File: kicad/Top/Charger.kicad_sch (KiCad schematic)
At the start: 37 parts

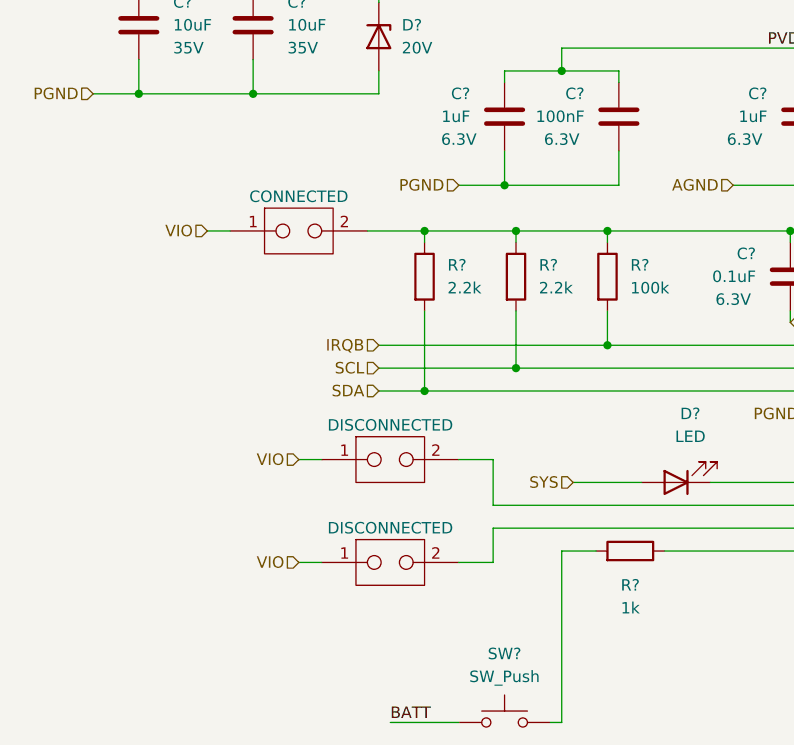
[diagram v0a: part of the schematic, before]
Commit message: replaced all shunt jumpers with better symbols
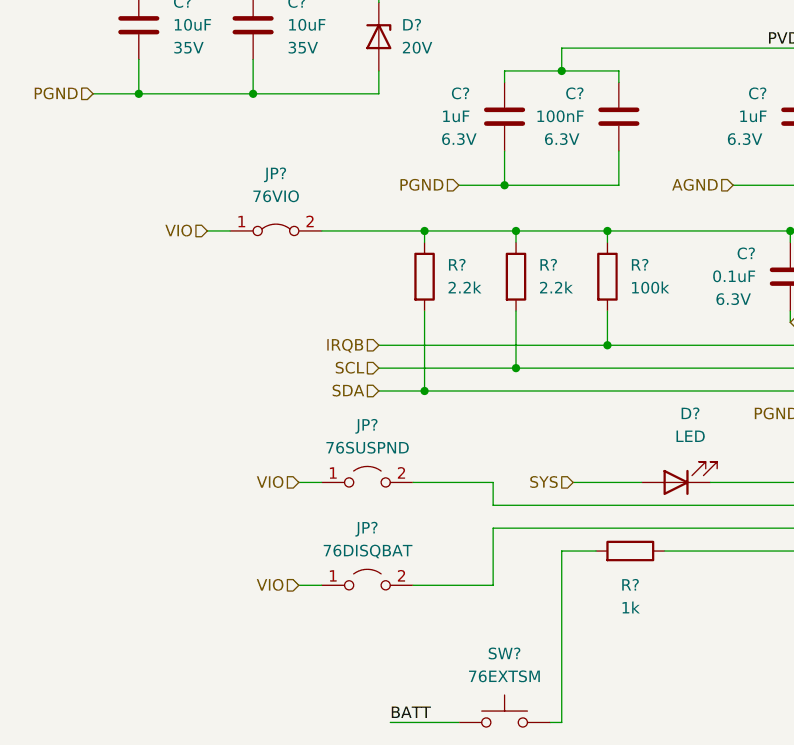
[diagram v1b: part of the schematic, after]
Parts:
- removed CHG_DISQBAT, CHG_SUSPND: DISCONNECTED, custom_connectors:2.54mm_2pointCurrentTestPoint, symbol custom_connectors:TestPoint_CurrentShunt
- removed CHG_VIO: CONNECTED, custom_connectors:2.54mm_2pointCurrentTestPoint, symbol custom_connectors:TestPoint_CurrentShunt
- added JP?: 76SUSPND, custom_connectors:2.54mm_2pointCurrentTestPoint, symbol Jumper:Jumper_2_Open
- added JP?: 76DISQBAT, custom_connectors:2.54mm_2pointCurrentTestPoint, symbol Jumper:Jumper_2_Open
- added JP?: 76VIO, custom_connectors:2.54mm_2pointCurrentTestPoint, symbol Jumper:Jumper_2_Bridged
- SW?: value SW_Push -> 76EXTSM
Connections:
- net VIO: now also JP?.1 (A), JP?.1 (A), JP?.1 (A)
- net at U?.1 (DISQBAT): now also JP?.2 (B)
- net at C?.1, R?.1, R?.1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: now also JP?.2 (B)
- net at U?.31 (SUSPND): now also JP?.2 (B)
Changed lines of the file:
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@@
+    (stroke (width 0) (type default) (color 0 0 0 0))
+  )
+  (wire (pts (xy 57.15 139.7) (xy 57.15 137.16))
     (stroke (width 0) (type default) (color 0 0 0 0))
   )
@@
     (stroke (width 0) (type default) (color 0 0 0 0))
   )
-  (wire (pts (xy 43.18 109.22) (xy 49.53 109.22))
+  (wire (pts (xy 38.1 109.22) (xy 49.53 109.22))
     (stroke (width 0) (type default) (color 0 0 0 0))
   )
@@
     (stroke (width 0) (type default) (color 0 0 0 0))
   )
-  (wire (pts (xy 57.15 134.62) (xy 57.15 139.7))
-    (stroke (width 0) (type default) (color 0 0 0 0))
-  )
   (wire (pts (xy 147.32 109.22) (xy 147.32 111.76))
     (stroke (width 0) (type default) (color 0 0 0 0))
@@
     (stroke (width 0) (type default) (color 0 0 0 0))
   )
-  (wire (pts (xy 53.34 134.62) (xy 57.15 134.62))
-    (stroke (width 0) (type default) (color 0 0 0 0))
-  )
   (wire (pts (xy 170.18 142.24) (xy 170.18 139.7))
     (stroke (width 0) (type default) (color 0 0 0 0))
@@
     (stroke (width 0) (type default) (color 0 0 0 0))
   )
-  (wire (pts (xy 57.15 142.24) (xy 57.15 146.05))
+  (wire (pts (xy 57.15 142.24) (xy 57.15 148.59))
     (stroke (width 0) (type default) (color 0 0 0 0))
   )
@@
     (stroke (width 0) (type default) (color 0 0 0 0))
   )
+  (wire (pts (xy 57.15 148.59) (xy 48.26 148.59))
+    (stroke (width 0) (type default) (color 0 0 0 0))
+  )
   (wire (pts (xy 147.32 124.46) (xy 147.32 127))
     (stroke (width 0) (type default) (color 0 0 0 0))
@@
     (stroke (width 0) (type default) (color 0 0 0 0))
   )
+  (wire (pts (xy 57.15 137.16) (xy 48.26 137.16))
+    (stroke (width 0) (type default) (color 0 0 0 0))
+  )
   (wire (pts (xy 168.91 152.4) (xy 170.18 152.4))
     (stroke (width 0) (type default) (color 0 0 0 0))
@@
     (stroke (width 0) (type default) (color 0 0 0 0))
   )
-  (wire (pts (xy 35.56 134.62) (xy 38.1 134.62))
+  (wire (pts (xy 35.56 137.16) (xy 38.1 137.16))
     (stroke (width 0) (type default) (color 0 0 0 0))
   )
@@
     (stroke (width 0) (type default) (color 0 0 0 0))
   )
-  (wire (pts (xy 57.15 146.05) (xy 53.34 146.05))
-    (stroke (width 0) (type default) (color 0 0 0 0))
-  )
   (wire (pts (xy 264.16 106.68) (xy 264.16 109.22))
     (stroke (width 0) (type default) (color 0 0 0 0))
@@
     (stroke (width 0) (type default) (color 0 0 0 0))
   )
-  (wire (pts (xy 35.56 146.05) (xy 38.1 146.05))
+  (wire (pts (xy 35.56 148.59) (xy 38.1 148.59))
     (stroke (width 0) (type default) (color 0 0 0 0))
   )
@@
     (effects (font (size 1.27 1.27)) (justify right))
   )
-  (hierarchical_label "VIO" (shape input) (at 35.56 134.62 180)
+  (hierarchical_label "VIO" (shape input) (at 35.56 137.16 180)
     (effects (font (size 1.27 1.27)) (justify right))
   )
@@
     (effects (font (size 1.27 1.27)) (justify left))
   )
-  (hierarchical_label "VIO" (shape input) (at 35.56 146.05 180)
+  (hierarchical_label "VIO" (shape input) (at 35.56 148.59 180)
     (effects (font (size 1.27 1.27)) (justify right))
   )
@@
   (hierarchical_label "IRQB" (shape input) (at 44.45 121.92 180)
     (effects (font (size 1.27 1.27)) (justify right))
-  )
-  (symbol (lib_id "custom_connectors:TestPoint_CurrentShunt") (at 45.72 146.05 0) (unit 1)
-    (in_bom yes) (on_board yes) (fields_autoplaced)
-    (property "Reference" "CHG_DISQBAT" (id 0) (at 45.72 140.97 0)
-      (effects (font (size 1.27 1.27)) hide)
-    )
-    (property "Value" "DISCONNECTED" (id 1) (at 45.72 142.24 0))
-    (property "Footprint" "custom_connectors:2.54mm_2pointCurrentTestPoint" (id 2) (at 45.72 146.05 0)
-      (effects (font (size 1.27 1.27)) hide)
-    )
-    (property "Datasheet" "https://www.digikey.jp/product-detail/en/kycon-inc/SX1100-B/2092-SX1100-B-ND/9990206" (id 3) (at 45.72 146.05 0)
-      (effects (font (size 1.27 1.27)) hide)
-    )
-    (pin "1")
-    (pin "2")
   )
   (symbol (lib_id "Device:C") (at 191.77 128.27 0) (mirror y) (unit 1)
@@
     (pin "2")
   )
+  (symbol (lib_id "Jumper:Jumper_2_Open") (at 43.18 137.16 0) (unit 1)
+    (in_bom yes) (on_board yes) (fields_autoplaced)
+    (property "Reference" "JP?" (id 0) (at 43.18 130.81 0))
+    (property "Value" "76SUSPND" (id 1) (at 43.18 133.35 0))
+    (property "Footprint" "custom_connectors:2.54mm_2pointCurrentTestPoint" (id 2) (at 43.18 137.16 0)
+      (effects (font (size 1.27 1.27)) hide)
+    )
+    (property "Datasheet" "~" (id 3) (at 43.18 137.16 0)
+      (effects (font (size 1.27 1.27)) hide)
+    )
+    (property "Description" "2.54mm male header with jumper absent" (id 4) (at 43.18 137.16 0)
+      (effects (font (size 1.27 1.27)) hide)
+    )
+    (pin "1")
+    (pin "2")
+  )
+  (symbol (lib_id "Jumper:Jumper_2_Open") (at 43.18 148.59 0) (unit 1)
+    (in_bom yes) (on_board yes) (fields_autoplaced)
+    (property "Reference" "JP?" (id 0) (at 43.18 142.24 0))
+    (property "Value" "76DISQBAT" (id 1) (at 43.18 144.78 0))
+    (property "Footprint" "custom_connectors:2.54mm_2pointCurrentTestPoint" (id 2) (at 43.18 148.59 0)
+      (effects (font (size 1.27 1.27)) hide)
+    )
+    (property "Datasheet" "~" (id 3) (at 43.18 148.59 0)
+      (effects (font (size 1.27 1.27)) hide)
+    )
+    (property "Description" "2.54mm male header with jumper absent" (id 4) (at 43.18 148.59 0)
+      (effects (font (size 1.27 1.27)) hide)
+    )
+    (pin "1")
+    (pin "2")
+  )
   (symbol (lib_id "pspice:INDUCTOR") (at 171.45 99.06 0) (unit 1)
     (in_bom yes) (on_board yes)
@@
     (pin "2")
   )
+  (symbol (lib_id "Jumper:Jumper_2_Bridged") (at 33.02 109.22 0) (unit 1)
+    (in_bom yes) (on_board yes) (fields_autoplaced)
+    (property "Reference" "JP?" (id 0) (at 33.02 102.87 0))
+    (property "Value" "76VIO" (id 1) (at 33.02 105.41 0))
+    (property "Footprint" "custom_connectors:2.54mm_2pointCurrentTestPoint" (id 2) (at 33.02 109.22 0)
+      (effects (font (size 1.27 1.27)) hide)
+    )
+    (property "Datasheet" "~" (id 3) (at 33.02 109.22 0)
+      (effects (font (size 1.27 1.27)) hide)
+    )
+    (property "Description" "2.54mm male header with jumper attached" (id 4) (at 33.02 109.22 0)
+      (effects (font (size 1.27 1.27)) hide)
+    )
+    (pin "1")
+    (pin "2")
+  )
   (symbol (lib_id "Connector:TestPoint") (at 91.44 81.28 0) (unit 1)
     (in_bom yes) (on_board yes) (fields_autoplaced)
@@
     )
     (property "Description" "6.3V" (id 4) (at 53.34 99.06 0))
-    (pin "1")
-    (pin "2")
-  )
-  (symbol (lib_id "custom_connectors:TestPoint_CurrentShunt") (at 35.56 109.22 0) (unit 1)
-    (in_bom yes) (on_board yes) (fields_autoplaced)
-    (property "Reference" "CHG_VIO" (id 0) (at 35.56 104.14 0)
-      (effects (font (size 1.27 1.27)) hide)
-    )
-    (property "Value" "CONNECTED" (id 1) (at 35.56 105.41 0))
-    (property "Footprint" "custom_connectors:2.54mm_2pointCurrentTestPoint" (id 2) (at 35.56 109.22 0)
-      (effects (font (size 1.27 1.27)) hide)
-    )
-    (property "Datasheet" "https://www.digikey.jp/product-detail/en/kycon-inc/SX1100-B/2092-SX1100-B-ND/9990206" (id 3) (at 35.56 109.22 0)
-      (effects (font (size 1.27 1.27)) hide)
-    )
     (pin "1")
     (pin "2")
@@
     (pin "2")
   )
-  (symbol (lib_id "custom_connectors:TestPoint_CurrentShunt") (at 45.72 134.62 0) (unit 1)
-    (in_bom yes) (on_board yes) (fields_autoplaced)
-    (property "Reference" "CHG_SUSPND" (id 0) (at 45.72 129.54 0)
-      (effects (font (size 1.27 1.27)) hide)
-    )
-    (property "Value" "DISCONNECTED" (id 1) (at 45.72 130.81 0))
-    (property "Footprint" "custom_connectors:2.54mm_2pointCurrentTestPoint" (id 2) (at 45.72 134.62 0)
-      (effects (font (size 1.27 1.27)) hide)
-    )
-    (property "Datasheet" "https://www.digikey.jp/product-detail/en/kycon-inc/SX1100-B/2092-SX1100-B-ND/9990206" (id 3) (at 45.72 134.62 0)
-      (effects (font (size 1.27 1.27)) hide)
-    )
-    (pin "1")
-    (pin "2")
-  )
   (symbol (lib_id "Device:C") (at 213.36 128.27 0) (mirror y) (unit 1)
     (in_bom yes) (on_board no)
@@
     (in_bom yes) (on_board yes) (fields_autoplaced)
     (property "Reference" "SW?" (id 0) (at 58.42 156.21 0))
-    (property "Value" "SW_Push" (id 1) (at 58.42 158.75 0))
+    (property "Value" "76EXTSM" (id 1) (at 58.42 158.75 0))
     (property "Footprint" "" (id 2) (at 58.42 158.75 0)
       (effects (font (size 1.27 1.27)) hide)

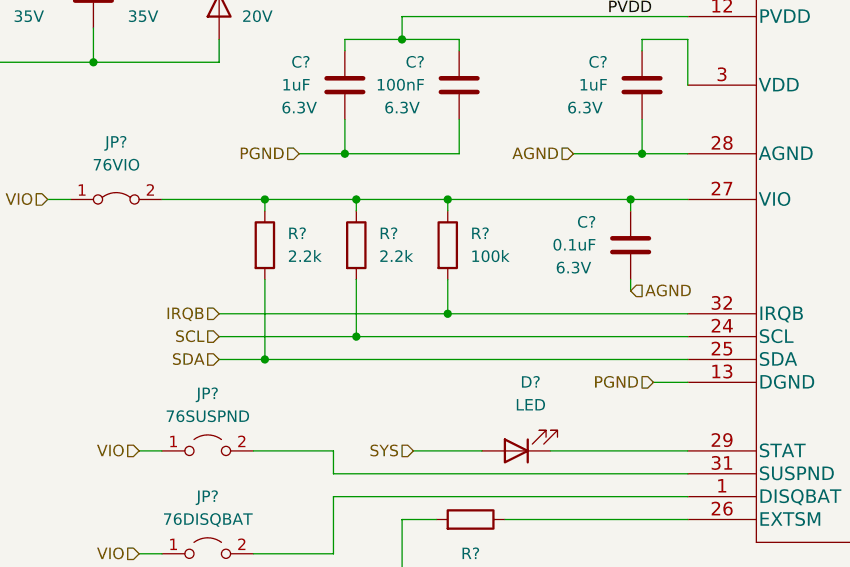
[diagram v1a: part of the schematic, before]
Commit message: Removed pull ups from battery charger
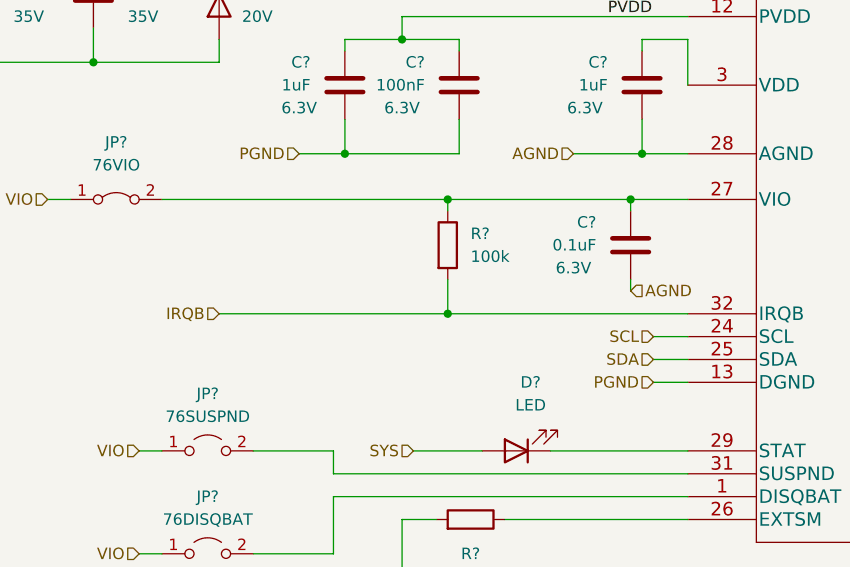
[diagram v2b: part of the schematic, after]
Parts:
- removed R? (x2): 2.2k, symbol Device:R
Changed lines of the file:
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@@
   (junction (at 224.79 99.06) (diameter 0) (color 0 0 0 0)
   )
-  (junction (at 49.53 109.22) (diameter 0) (color 0 0 0 0)
-  )
   (junction (at 224.79 109.22) (diameter 0) (color 0 0 0 0)
   )
-  (junction (at 59.69 124.46) (diameter 0) (color 0 0 0 0)
-  )
   (junction (at 73.66 81.28) (diameter 0) (color 0 0 0 0)
   )
@@
   (junction (at 91.44 81.28) (diameter 0) (color 0 0 0 0)
   )
-  (junction (at 49.53 127) (diameter 0) (color 0 0 0 0)
-  )
   (junction (at 90.17 109.22) (diameter 0) (color 0 0 0 0)
   )
   (junction (at 205.74 109.22) (diameter 0) (color 0 0 0 0)
-  )
-  (junction (at 59.69 109.22) (diameter 0) (color 0 0 0 0)
   )
   (junction (at 147.32 96.52) (diameter 0) (color 0 0 0 0)
@@
     (stroke (width 0) (type default) (color 0 0 0 0))
   )
-  (wire (pts (xy 59.69 110.49) (xy 59.69 109.22))
-    (stroke (width 0) (type default) (color 0 0 0 0))
-  )
   (wire (pts (xy 57.15 139.7) (xy 57.15 137.16))
     (stroke (width 0) (type default) (color 0 0 0 0))
@@
     (stroke (width 0) (type default) (color 0 0 0 0))
   )
-  (wire (pts (xy 38.1 109.22) (xy 49.53 109.22))
+  (wire (pts (xy 38.1 109.22) (xy 69.85 109.22))
     (stroke (width 0) (type default) (color 0 0 0 0))
   )
@@
     (stroke (width 0) (type default) (color 0 0 0 0))
   )
-  (wire (pts (xy 49.53 127) (xy 49.53 118.11))
-    (stroke (width 0) (type default) (color 0 0 0 0))
-  )
   (wire (pts (xy 44.45 93.98) (xy 30.48 93.98))
     (stroke (width 0) (type default) (color 0 0 0 0))
@@
     (stroke (width 0) (type default) (color 0 0 0 0))
   )
-  (wire (pts (xy 59.69 109.22) (xy 69.85 109.22))
-    (stroke (width 0) (type default) (color 0 0 0 0))
-  )
   (wire (pts (xy 96.52 81.28) (xy 96.52 83.82))
     (stroke (width 0) (type default) (color 0 0 0 0))
@@
     (stroke (width 0) (type default) (color 0 0 0 0))
   )
-  (wire (pts (xy 49.53 127) (xy 96.52 127))
+  (wire (pts (xy 92.71 127) (xy 96.52 127))
     (stroke (width 0) (type default) (color 0 0 0 0))
   )
@@
     (stroke (width 0) (type default) (color 0 0 0 0))
   )
-  (wire (pts (xy 44.45 127) (xy 49.53 127))
-    (stroke (width 0) (type default) (color 0 0 0 0))
-  )
   (wire (pts (xy 147.32 119.38) (xy 182.88 119.38))
     (stroke (width 0) (type default) (color 0 0 0 0))
@@
     (stroke (width 0) (type default) (color 0 0 0 0))
   )
-  (wire (pts (xy 44.45 124.46) (xy 59.69 124.46))
-    (stroke (width 0) (type default) (color 0 0 0 0))
-  )
   (wire (pts (xy 220.98 152.4) (xy 226.06 152.4))
     (stroke (width 0) (type default) (color 0 0 0 0))
@@
     (stroke (width 0) (type default) (color 0 0 0 0))
   )
-  (wire (pts (xy 59.69 124.46) (xy 96.52 124.46))
+  (wire (pts (xy 92.71 124.46) (xy 96.52 124.46))
     (stroke (width 0) (type default) (color 0 0 0 0))
   )
@@
     (stroke (width 0) (type default) (color 0 0 0 0))
   )
-  (wire (pts (xy 59.69 124.46) (xy 59.69 118.11))
-    (stroke (width 0) (type default) (color 0 0 0 0))
-  )
   (wire (pts (xy 147.32 124.46) (xy 191.77 124.46))
     (stroke (width 0) (type default) (color 0 0 0 0))
   )
-  (wire (pts (xy 49.53 110.49) (xy 49.53 109.22))
-    (stroke (width 0) (type default) (color 0 0 0 0))
-  )
   (wire (pts (xy 53.34 104.14) (xy 58.42 104.14))
     (stroke (width 0) (type default) (color 0 0 0 0))
@@
   )
   (wire (pts (xy 90.17 118.11) (xy 90.17 119.38))
-    (stroke (width 0) (type default) (color 0 0 0 0))
-  )
-  (wire (pts (xy 49.53 109.22) (xy 59.69 109.22))
     (stroke (width 0) (type default) (color 0 0 0 0))
   )
@@
     (effects (font (size 1.27 1.27)) (justify right))
   )
-  (hierarchical_label "SCL" (shape input) (at 44.45 124.46 180)
+  (hierarchical_label "SCL" (shape input) (at 92.71 124.46 180)
     (effects (font (size 1.27 1.27)) (justify right))
   )
@@
     (effects (font (size 1.27 1.27)) (justify right))
   )
-  (hierarchical_label "SDA" (shape input) (at 44.45 127 180)
+  (hierarchical_label "SDA" (shape input) (at 92.71 127 180)
     (effects (font (size 1.27 1.27)) (justify right))
   )
@@
     (property "Description" "35V" (id 4) (at 34.29 88.8999 0)
       (effects (font (size 1.27 1.27)) (justify left))
-    )
-    (pin "1")
-    (pin "2")
-  )
-  (symbol (lib_id "Device:R") (at 49.53 114.3 0) (unit 1)
-    (in_bom yes) (on_board yes) (fields_autoplaced)
-    (property "Reference" "R?" (id 0) (at 52.07 113.0299 0)
-      (effects (font (size 1.27 1.27)) (justify left))
-    )
-    (property "Value" "2.2k" (id 1) (at 52.07 115.5699 0)
-      (effects (font (size 1.27 1.27)) (justify left))
-    )
-    (property "Footprint" "" (id 2) (at 47.752 114.3 90)
-      (effects (font (size 1.27 1.27)) hide)
-    )
-    (property "Datasheet" "~" (id 3) (at 49.53 114.3 0)
-      (effects (font (size 1.27 1.27)) hide)
     )
     (pin "1")
@@
     )
     (pin "1")
-    (pin "2")
-  )
-  (symbol (lib_id "Device:R") (at 59.69 114.3 0) (unit 1)
-    (in_bom yes) (on_board yes) (fields_autoplaced)
-    (property "Reference" "R?" (id 0) (at 62.23 113.0299 0)
-      (effects (font (size 1.27 1.27)) (justify left))
-    )
-    (property "Value" "2.2k" (id 1) (at 62.23 115.5699 0)
-      (effects (font (size 1.27 1.27)) (justify left))
-    )
-    (property "Footprint" "" (id 2) (at 57.912 114.3 90)
-      (effects (font (size 1.27 1.27)) hide)
-    )
-    (property "Datasheet" "~" (id 3) (at 59.69 114.3 0)
-      (effects (font (size 1.27 1.27)) hide)
-    )
-    (pin "1")
